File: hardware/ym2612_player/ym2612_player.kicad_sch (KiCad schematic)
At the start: 0 parts

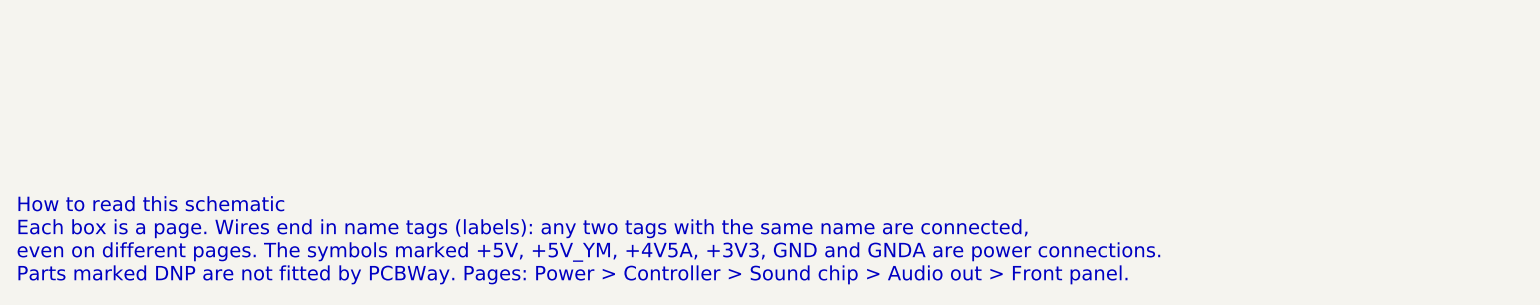
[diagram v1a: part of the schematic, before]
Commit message: Apply the Rev A fix register: decoupling, single ground, A.VCC filter, TPA6132A2
Schematic
- YM2612 A.VCC (pin 22) gets its own 10 ohm + 220 uF + 100 nF filter.
- /IC, A0, A1 pull-downs 10k -> 4.7k (RP2350 erratum E9).
- Headphone amp: NJM4556A replaced by a TPA6132A2 at -6 dB, no output caps,
  enabled by GP12 (HP_EN, 4.7k pull-down) so power-up doesn't pop.
- 47 uF electrolytic damps the L1/C4 resonance before the LP5907.
- GNDA merged into GND; NT1 removed. Four M3 holes for the LCD standoffs.
- Ferrite label 220R@100MHz to match BLM18PG221SN1D; C15/C22 spec X7R 50V;
  LED lead note for PCBWay.
- Pico Plus 2 and its headers marked do-not-fit (Joey supplies them);
  sockets are Sullins PPTC201LFBN-RC.

Layout
- Decoupling caps placed at the pin they serve (design.NEAR), 2-7 mm instead
  of 16-70 mm.
- One solid GND plane on both layers plus 332 stitching vias (tools/stitch.py).
- J6 moved out from under the LCD backpack; encoder moved below the LCD so
  the knob clears it.
- Re-routed with Freerouting; KiCad 7 DRC: 0 errors, 0 unconnected.

Co-Authored-By: Claude Opus 5.5 (1M context) <noreply@anthropic.com>
Claude-Session: https://claude.ai/code/session_01T6y8roX1LzS9uTuKVQBe9X
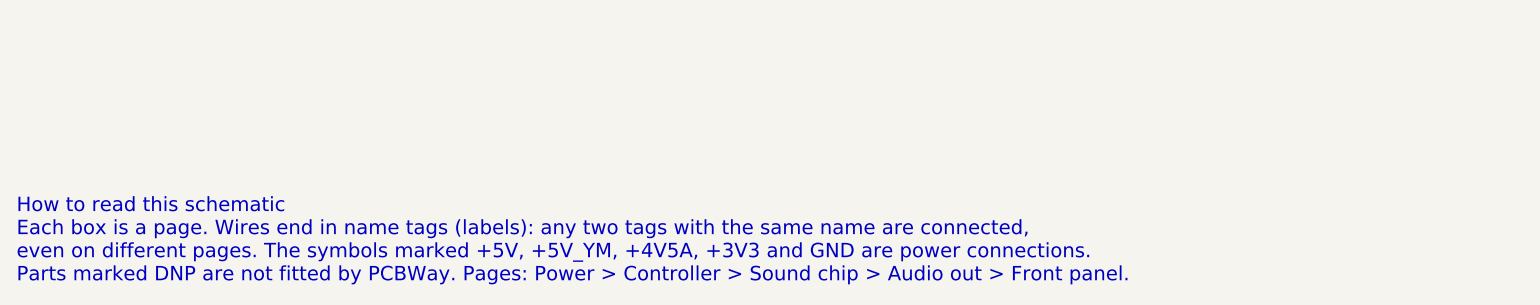
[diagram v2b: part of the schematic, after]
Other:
- note added: "How to read this schematic Each box is a page. Wires end in name tags (labels): any two tags with the same name are connected, even on different pages. The symbols marked +5V, +5V_YM, +4V5A, +3V3 and GND are power connections. Parts marked DNP are not fitted by PCBWay. Pages: Power > Controller > Sound chip > Audio out > Front panel."
- note removed: "How to read this schematic Each box is a page. Wires end in name tags (labels): any two tags with the same name are connected, even on different pages. The symbols marked +5V, +5V_YM, +4V5A, +3V3, GND and GNDA are power connections. Parts marked DNP are not fitted by PCBWay. Pages: Power > Controller > Sound chip > Audio out > Front panel."
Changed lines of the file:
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@@
     )
   )
-  (text "How to read this schematic\nEach box is a page. Wires end in name tags (labels): any two tags with the same name are connected,\neven on different pages. The symbols marked +5V, +5V_YM, +4V5A, +3V3, GND and GNDA are power connections.\nParts marked DNP are not fitted by PCBWay. Pages: Power > Controller > Sound chip > Audio out > Front panel." (at 30.48 140 0)
+  (text "How to read this schematic\nEach box is a page. Wires end in name tags (labels): any two tags with the same name are connected,\neven on different pages. The symbols marked +5V, +5V_YM, +4V5A, +3V3 and GND are power connections.\nParts marked DNP are not fitted by PCBWay. Pages: Power > Controller > Sound chip > Audio out > Front panel." (at 30.48 140 0)
     (effects (font (size 1.8 1.8)) (justify left top))
   )

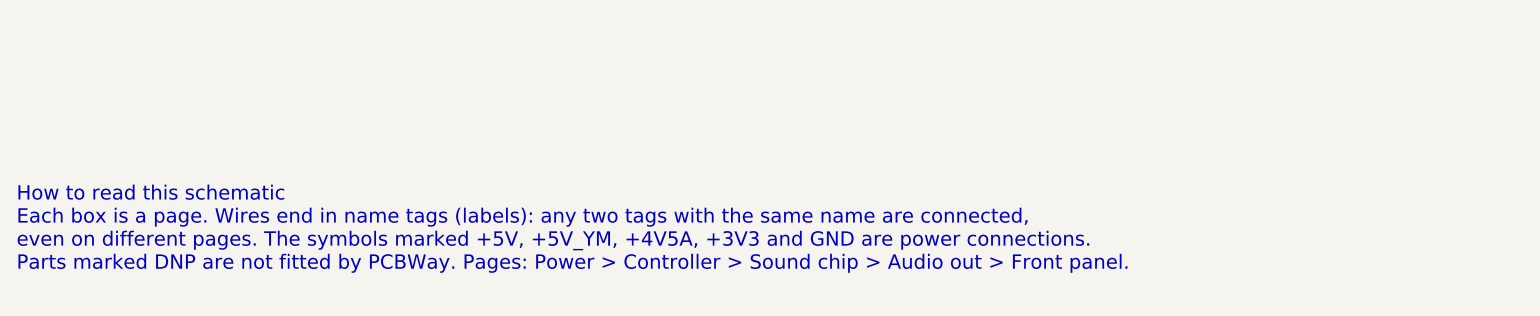
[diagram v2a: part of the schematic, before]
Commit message: Schematic: draw real wires between parts instead of name tags
tools/wires.py routes each page's nets on the 1.27 mm grid around part bodies and text.
Power pins keep power symbols (neighbouring pins share one), signals that leave a page get
one global label, and the netlist check still matches design.py exactly (0 mismatches).
Sound chip and audio pages re-laid out so the wiring reads left to right; title blocks say Rev B.

Co-Authored-By: Claude Opus 5.5 <noreply@anthropic.com>
Claude-Session: https://claude.ai/code/session_01TDTDVidYRoyJdUGgsyVTSw
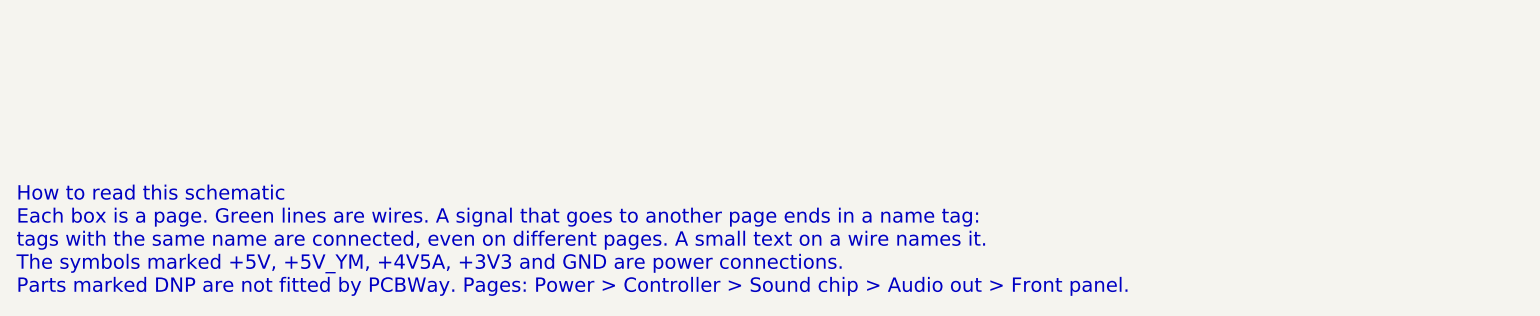
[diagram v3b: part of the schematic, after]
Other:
- note added: "How to read this schematic Each box is a page. Green lines are wires. A signal that goes to another page ends in a name tag: tags with the same name are connected, even on different pages. A small text on a wire names it. The symbols marked +5V, +5V_YM, +4V5A, +3V3 and GND are power connections. Parts marked DNP are not fitted by PCBWay. Pages: Power > Controller > Sound chip > Audio out > Front 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"
- note removed: "How to read this schematic Each box is a page. Wires end in name tags (labels): any two tags with the same name are connected, even on different pages. The symbols marked +5V, +5V_YM, +4V5A, +3V3 and GND are power connections. Parts marked DNP are not fitted by PCBWay. Pages: Power > Controller > Sound chip > Audio out > Front panel."
- title: YM2612 player Rev A -> YM2612 player Rev B
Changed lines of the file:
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@@
   (paper "A4")
   (title_block
-    (title "YM2612 player Rev A")
-    (date "2026-10-24")
-    (rev "A0.1")
+    (title "YM2612 player Rev B")
+    (date "2026-10-31")
+    (rev "B0.1")
     (company "YM2612")
     (comment 1 "Top sheet: double-click a box to open that page")
@@
     )
   )
-  (text "How to read this schematic\nEach box is a page. Wires end in name tags (labels): any two tags with the same name are connected,\neven on different pages. The symbols marked +5V, +5V_YM, +4V5A, +3V3 and GND are power connections.\nParts marked DNP are not fitted by PCBWay. Pages: Power > Controller > Sound chip > Audio out > Front panel." (at 30.48 140 0)
+  (text "How to read this schematic\nEach box is a page. Green lines are wires. A signal that goes to another page ends in a name tag:\ntags with the same name are connected, even on different pages. A small text on a wire names it.\nThe symbols marked +5V, +5V_YM, +4V5A, +3V3 and GND are power connections.\nParts marked DNP are not fitted by PCBWay. Pages: Power > Controller > Sound chip > Audio out > Front panel." (at 30.48 140 0)
     (effects (font (size 1.8 1.8)) (justify left top))
   )
